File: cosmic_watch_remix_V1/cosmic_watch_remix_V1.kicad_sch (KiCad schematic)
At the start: 26 parts, among them IC1 MICROFJ-60035-TSV-TR1, IC2 LT3461AES6#TRMPBF, J1 Conn_01x05_Female, U1 ADS1115IDGS, U2 LM358

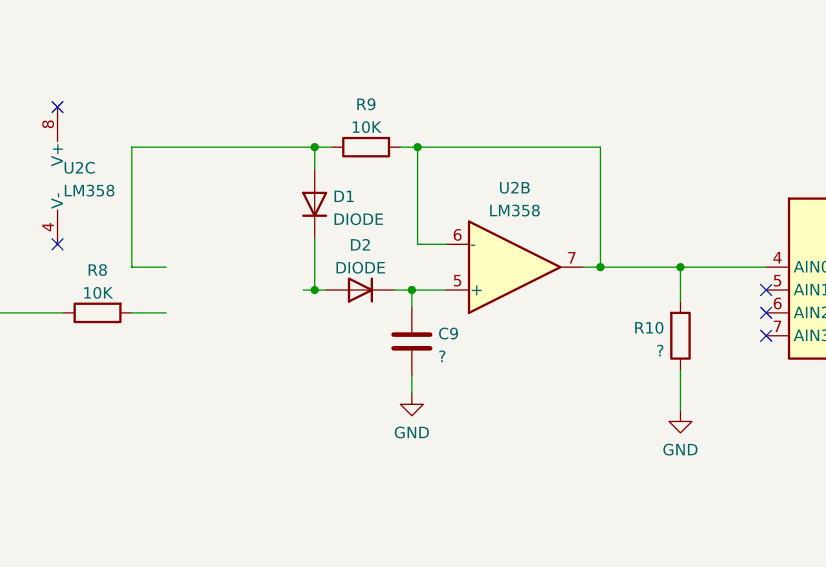
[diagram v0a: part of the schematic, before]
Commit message: Completed Component Selection
Note change to 28V output
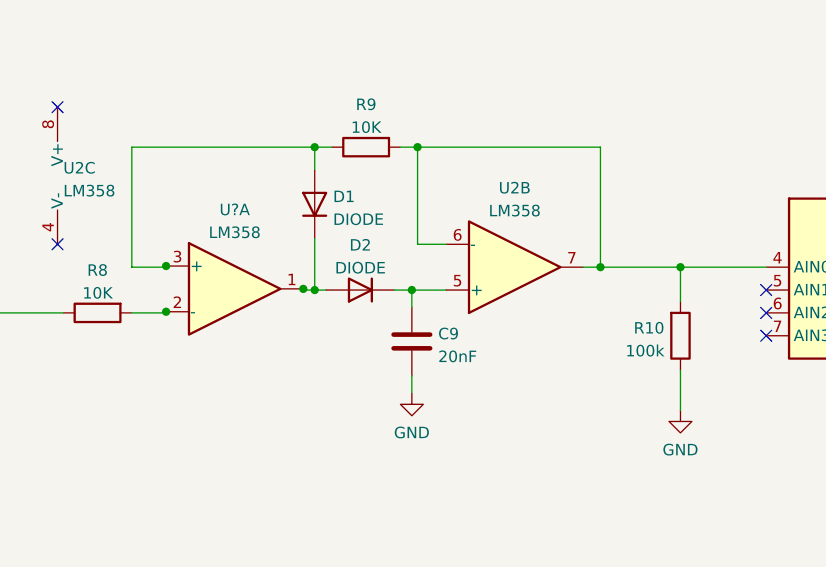
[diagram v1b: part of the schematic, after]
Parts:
- added U?: LM358, symbol Amplifier_Operational:LM358
- C9: value ? -> 20nF
- R10: value ? -> 100k
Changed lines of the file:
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@@
   (junction (at 39.37 128.27) (diameter 0) (color 0 0 0 0)
   )
+  (junction (at 140.97 90.678) (diameter 0) (color 0 0 0 0)
+  )
   (junction (at 99.06 105.41) (diameter 0) (color 0 0 0 0)
   )
@@
   (junction (at 26.035 41.91) (diameter 0) (color 0 0 0 0)
   )
+  (junction (at 125.73 93.218) (diameter 0) (color 0 0 0 0)
+  )
   (junction (at 99.06 135.89) (diameter 0) (color 0 0 0 0)
   )
@@
   )
   (junction (at 33.655 26.67) (diameter 0) (color 0 0 0 0)
+  )
+  (junction (at 125.73 88.138) (diameter 0) (color 0 0 0 0)
   )
   (no_connect (at 192.405 90.805))
@@
     (pin "2")
   )
+  (symbol (lib_id "Amplifier_Operational:LM358") (at 133.35 90.678 0) (unit 1)
+    (in_bom yes) (on_board yes) (fields_autoplaced)
+    (property "Reference" "U?" (id 0) (at 133.35 81.8982 0))
+    (property "Value" "LM358" (id 1) (at 133.35 84.4351 0))
+    (property "Footprint" "" (id 2) (at 133.35 90.678 0)
+      (effects (font (size 1.27 1.27)) hide)
+    )
+    (property "Datasheet" "http://www.ti.com/lit/ds/symlink/lm2904-n.pdf" (id 3) (at 133.35 90.678 0)
+      (effects (font (size 1.27 1.27)) hide)
+    )
+    (pin "1")
+    (pin "2")
+    (pin "3")
+  )
   (symbol (lib_id "power:GND") (at 182.88 104.14 0) (unit 1)
     (in_bom yes) (on_board yes) (fields_autoplaced)
@@
       (effects (font (size 1.27 1.27)) (justify left))
     )
-    (property "Value" "?" (id 1) (at 155.956 98.2222 0)
+    (property "Value" "20nF" (id 1) (at 155.956 98.2222 0)
       (effects (font (size 1.27 1.27)) (justify left))
     )
@@
   (symbol (lib_id "Device:R") (at 182.88 95.885 0) (mirror x) (unit 1)
     (in_bom yes) (on_board yes) (fields_autoplaced)
-    (property "Reference" "R10" (id 0) (at 181.102 95.0503 0)
+    (property "Reference" "R10" (id 0) (at 181.1021 95.0503 0)
       (effects (font (size 1.27 1.27)) (justify right))
     )
-    (property "Value" "?" (id 1) (at 181.102 97.5872 0)
+    (property "Value" "100k" (id 1) (at 181.1021 97.5872 0)
       (effects (font (size 1.27 1.27)) (justify right))
     )
@@
     )
     (path "/8d129ac0-21e8-4168-b5e8-555f7b81464d"
-      (reference "C9") (unit 1) (value "?") (footprint "Capacitor_SMD:C_0603_1608Metric")
+      (reference "C9") (unit 1) (value "20nF") (footprint "Capacitor_SMD:C_0603_1608Metric")
     )
     (path "/10789bbb-c1d1-4df2-bd22-ae0dfea0e3cd"
@@
     )
     (path "/a57db792-acd1-4a7c-9f3f-af8789d22ea8"
-      (reference "R10") (unit 1) (value "?") (footprint "Resistor_SMD:R_0603_1608Metric")
+      (reference "R10") (unit 1) (value "100k") (footprint "Resistor_SMD:R_0603_1608Metric")
     )
     (path "/d4e5a639-c802-4fd5-bd43-bd9483f1fee3"
@@
       (reference "U2") (unit 3) (value "LM358") (footprint "Package_SO:SOIC-8_7.5x5.85mm_P1.27mm")
     )
-  )
+    (path "/2e435b0f-671e-4da0-9b1a-48c487e95e18"
+      (reference "U?") (unit 1) (value "LM358") (footprint "")
+    )
+  )

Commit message: Updated Production Files
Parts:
- C9: value 20nF -> 22nF
- R6: value 280K -> 220K
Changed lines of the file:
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@@
     (in_bom yes) (on_board yes) (fields_autoplaced)
     (property "Reference" "R6" (id 0) (at 47.625 48.6242 90))
-    (property "Value" "280K" (id 1) (at 47.625 51.1611 90))
+    (property "Value" "220K" (id 1) (at 47.625 51.1611 90))
     (property "Footprint" "Resistor_SMD:R_0603_1608Metric" (id 2) (at 47.625 51.562 90)
       (effects (font (size 1.27 1.27)) hide)
@@
       (effects (font (size 1.27 1.27)) (justify left))
     )
-    (property "Value" "20nF" (id 1) (at 155.956 98.2222 0)
+    (property "Value" "22nF" (id 1) (at 155.956 98.2222 0)
       (effects (font (size 1.27 1.27)) (justify left))
     )
@@
     )
     (path "/8d129ac0-21e8-4168-b5e8-555f7b81464d"
-      (reference "C9") (unit 1) (value "20nF") (footprint "Capacitor_SMD:C_0603_1608Metric")
+      (reference "C9") (unit 1) (value "22nF") (footprint "Capacitor_SMD:C_0603_1608Metric")
     )
     (path "/10789bbb-c1d1-4df2-bd22-ae0dfea0e3cd"
@@
     )
     (path "/8c8f7f6f-f151-43d0-b7c2-857bd66addff"
-      (reference "R6") (unit 1) (value "280K") (footprint "Resistor_SMD:R_0603_1608Metric")
+      (reference "R6") (unit 1) (value "220K") (footprint "Resistor_SMD:R_0603_1608Metric")
     )
     (path "/b047d4a8-77a5-43d5-bbbe-e454ef0e254d"

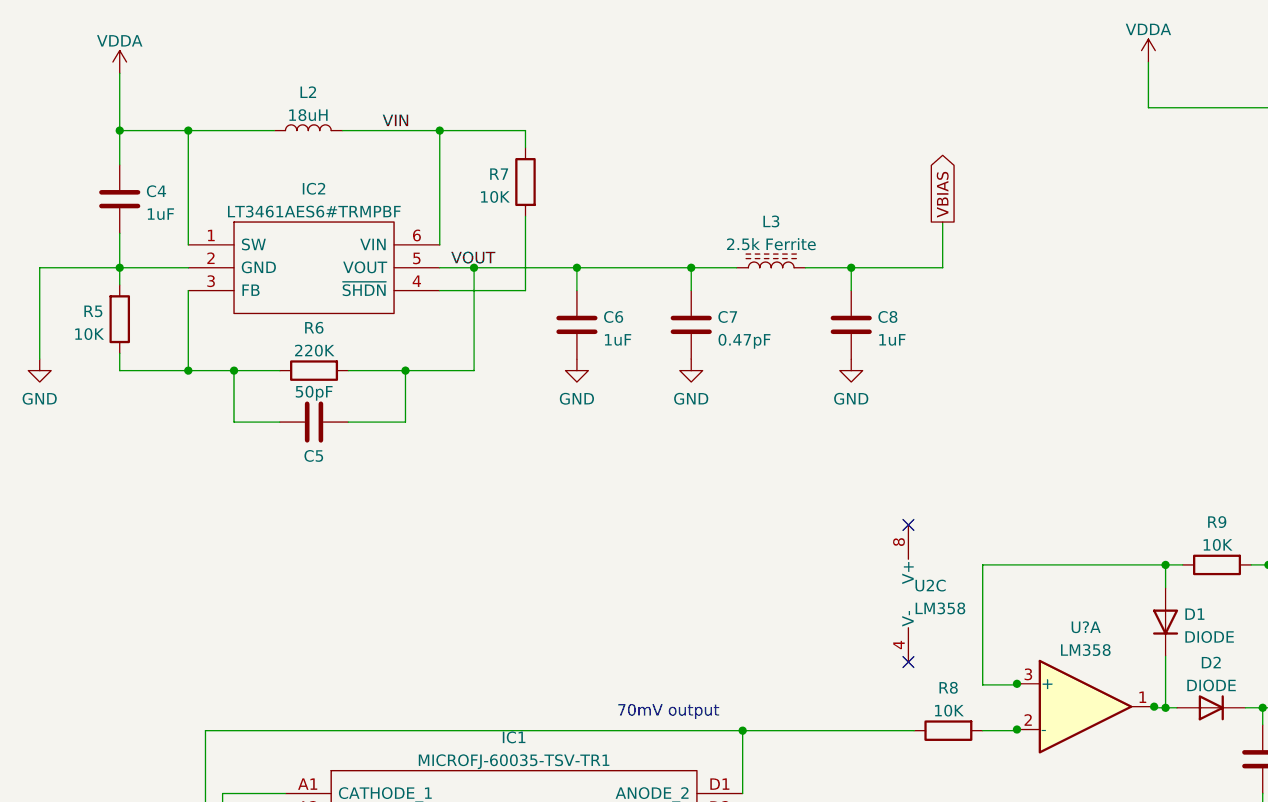
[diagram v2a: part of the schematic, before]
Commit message: Fixed Inductor Power Path
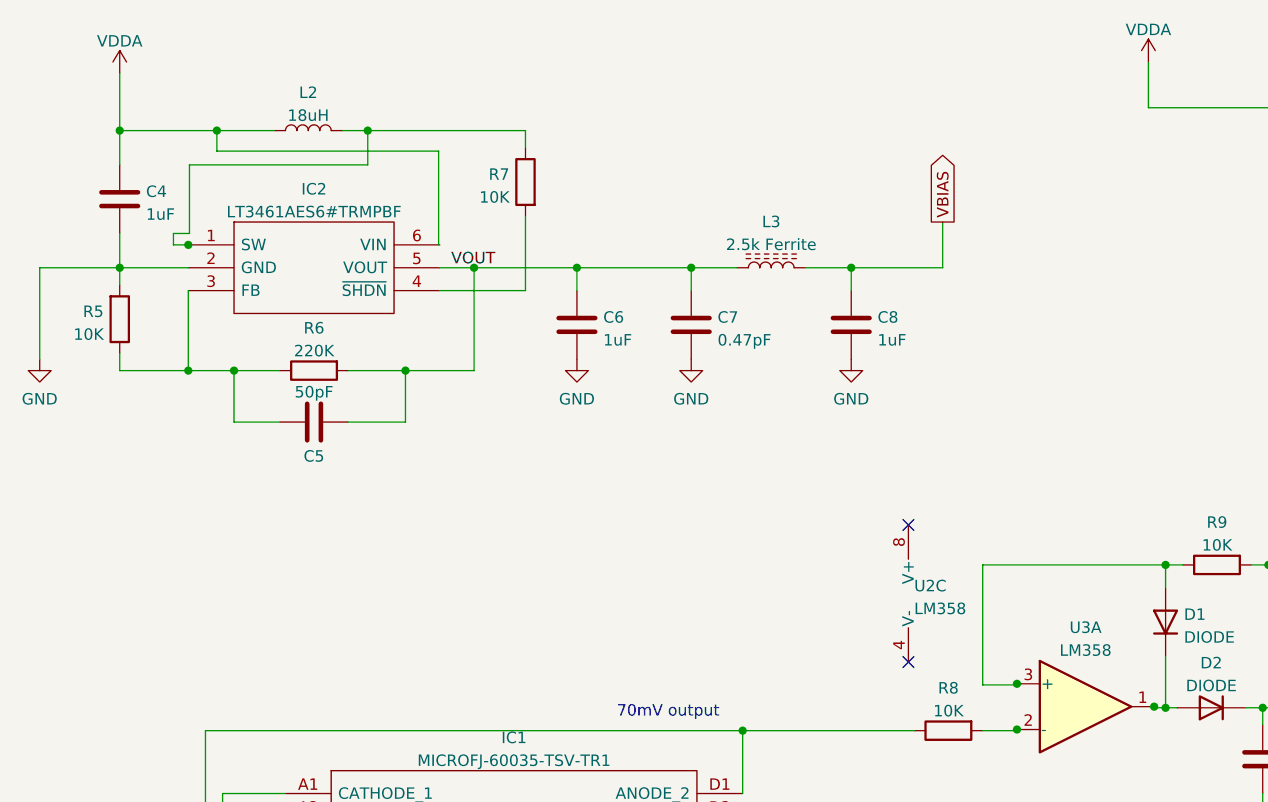
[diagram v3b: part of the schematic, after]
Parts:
- gave numbers to parts that had none: 1
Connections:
- net VCC: no longer IC2.1 (SW)
- net VIN: no longer names the net of L2.2, R7.1
- net VIN: now also IC2.1 (SW); no longer IC2.6 (VIN)
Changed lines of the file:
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@@
   (junction (at 95.25 93.345) (diameter 0) (color 0 0 0 0)
   )
+  (junction (at 33.655 39.37) (diameter 0) (color 0 0 0 0)
+  )
   (junction (at 241.935 93.345) (diameter 0) (color 0 0 0 0)
   )
   (junction (at 39.37 133.35) (diameter 0) (color 0 0 0 0)
   )
-  (junction (at 61.595 26.67) (diameter 0) (color 0 0 0 0)
-  )
   (junction (at 99.06 118.11) (diameter 0) (color 0 0 0 0)
   )
@@
   (junction (at 33.655 53.34) (diameter 0) (color 0 0 0 0)
   )
+  (junction (at 53.594 26.67) (diameter 0) (color 0 0 0 0)
+  )
   (junction (at 99.06 125.73) (diameter 0) (color 0 0 0 0)
   )
@@
   (junction (at 99.06 133.35) (diameter 0) (color 0 0 0 0)
   )
+  (junction (at 36.83 26.67) (diameter 0) (color 0 0 0 0)
+  )
   (junction (at 153.035 90.805) (diameter 0) (color 0 0 0 0)
   )
   (junction (at 173.99 88.265) (diameter 0) (color 0 0 0 0)
-  )
-  (junction (at 33.655 26.67) (diameter 0) (color 0 0 0 0)
   )
   (junction (at 125.73 88.138) (diameter 0) (color 0 0 0 0)
@@
     (stroke (width 0) (type default) (color 0 0 0 0))
   )
+  (wire (pts (xy 33.782 30.48) (xy 33.782 38.1))
+    (stroke (width 0) (type default) (color 0 0 0 0))
+  )
   (wire (pts (xy 39.37 135.89) (xy 39.37 138.43))
     (stroke (width 0) (type default) (color 0 0 0 0))
@@
     (stroke (width 0) (type default) (color 0 0 0 0))
   )
+  (wire (pts (xy 53.594 26.67) (xy 53.594 30.48))
+    (stroke (width 0) (type default) (color 0 0 0 0))
+  )
   (wire (pts (xy 99.06 105.41) (xy 99.06 107.95))
     (stroke (width 0) (type default) (color 0 0 0 0))
@@
     (stroke (width 0) (type default) (color 0 0 0 0))
   )
+  (wire (pts (xy 32.004 38.1) (xy 32.004 39.37))
+    (stroke (width 0) (type default) (color 0 0 0 0))
+  )
   (wire (pts (xy 173.99 74.93) (xy 153.67 74.93))
     (stroke (width 0) (type default) (color 0 0 0 0))
   )
+  (wire (pts (xy 36.83 28.956) (xy 36.83 26.67))
+    (stroke (width 0) (type default) (color 0 0 0 0))
+  )
   (wire (pts (xy 61.595 41.91) (xy 65.405 41.91))
     (stroke (width 0) (type default) (color 0 0 0 0))
@@
     (stroke (width 0) (type default) (color 0 0 0 0))
   )
+  (wire (pts (xy 33.655 39.37) (xy 33.782 39.37))
+    (stroke (width 0) (type default) (color 0 0 0 0))
+  )
   (wire (pts (xy 39.37 120.65) (xy 44.45 120.65))
     (stroke (width 0) (type default) (color 0 0 0 0))
@@
     (stroke (width 0) (type default) (color 0 0 0 0))
   )
-  (wire (pts (xy 71.12 26.67) (xy 61.595 26.67))
+  (wire (pts (xy 50.8 26.67) (xy 53.594 26.67))
+    (stroke (width 0) (type default) (color 0 0 0 0))
+  )
+  (wire (pts (xy 36.83 26.67) (xy 43.18 26.67))
     (stroke (width 0) (type default) (color 0 0 0 0))
   )
@@
     (stroke (width 0) (type default) (color 0 0 0 0))
   )
-  (wire (pts (xy 26.035 26.67) (xy 33.655 26.67))
-    (stroke (width 0) (type default) (color 0 0 0 0))
-  )
   (wire (pts (xy 39.37 110.49) (xy 39.37 113.03))
     (stroke (width 0) (type default) (color 0 0 0 0))
@@
     (stroke (width 0) (type default) (color 0 0 0 0))
   )
-  (wire (pts (xy 61.595 26.67) (xy 61.595 39.37))
-    (stroke (width 0) (type default) (color 0 0 0 0))
-  )
   (wire (pts (xy 95.25 115.57) (xy 99.06 115.57))
     (stroke (width 0) (type default) (color 0 0 0 0))
   )
-  (wire (pts (xy 50.8 26.67) (xy 61.595 26.67))
-    (stroke (width 0) (type default) (color 0 0 0 0))
-  )
   (wire (pts (xy 89.535 41.91) (xy 89.535 44.45))
     (stroke (width 0) (type default) (color 0 0 0 0))
@@
     (stroke (width 0) (type default) (color 0 0 0 0))
   )
-  (wire (pts (xy 33.655 26.67) (xy 43.18 26.67))
+  (wire (pts (xy 53.594 26.67) (xy 71.12 26.67))
+    (stroke (width 0) (type default) (color 0 0 0 0))
+  )
+  (wire (pts (xy 26.035 26.67) (xy 36.83 26.67))
     (stroke (width 0) (type default) (color 0 0 0 0))
   )
@@
     (stroke (width 0) (type default) (color 0 0 0 0))
   )
+  (wire (pts (xy 32.004 39.37) (xy 33.655 39.37))
+    (stroke (width 0) (type default) (color 0 0 0 0))
+  )
   (wire (pts (xy 95.25 105.41) (xy 99.06 105.41))
     (stroke (width 0) (type default) (color 0 0 0 0))
   )
+  (wire (pts (xy 61.468 28.956) (xy 36.83 28.956))
+    (stroke (width 0) (type default) (color 0 0 0 0))
+  )
   (wire (pts (xy 39.37 120.65) (xy 39.37 123.19))
     (stroke (width 0) (type default) (color 0 0 0 0))
@@
     (stroke (width 0) (type default) (color 0 0 0 0))
   )
+  (wire (pts (xy 33.782 38.1) (xy 32.004 38.1))
+    (stroke (width 0) (type default) (color 0 0 0 0))
+  )
   (wire (pts (xy 95.25 100.33) (xy 95.25 93.345))
     (stroke (width 0) (type default) (color 0 0 0 0))
@@
     (stroke (width 0) (type default) (color 0 0 0 0))
   )
+  (wire (pts (xy 61.468 39.37) (xy 61.468 28.956))
+    (stroke (width 0) (type default) (color 0 0 0 0))
+  )
   (wire (pts (xy 39.37 138.43) (xy 44.45 138.43))
     (stroke (width 0) (type default) (color 0 0 0 0))
@@
     (stroke (width 0) (type default) (color 0 0 0 0))
   )
+  (wire (pts (xy 53.594 30.48) (xy 33.782 30.48))
+    (stroke (width 0) (type default) (color 0 0 0 0))
+  )
   (wire (pts (xy 178.435 24.13) (xy 178.435 19.05))
     (stroke (width 0) (type default) (color 0 0 0 0))
@@
   )
   (wire (pts (xy 95.25 107.95) (xy 99.06 107.95))
-    (stroke (width 0) (type default) (color 0 0 0 0))
-  )
-  (wire (pts (xy 33.655 39.37) (xy 33.655 26.67))
     (stroke (width 0) (type default) (color 0 0 0 0))
   )
@@
   )
   (label "VOUT" (at 62.865 41.91 0)
-    (effects (font (size 1.27 1.27)) (justify left bottom))
-  )
-  (label "VIN" (at 55.245 26.67 0)
     (effects (font (size 1.27 1.27)) (justify left bottom))
   )
@@
       (effects (font (size 1.27 1.27)) hide)
     )
+    (pin "1")
+    (pin "2")
+    (pin "3")
+    (pin "5")
+    (pin "6")
+    (pin "7")
     (pin "4")
     (pin "8")
@@
   (symbol (lib_id "Amplifier_Operational:LM358") (at 133.35 90.678 0) (unit 1)
     (in_bom yes) (on_board yes) (fields_autoplaced)
-    (property "Reference" "U?" (id 0) (at 133.35 81.8982 0))
+    (property "Reference" "U3" (id 0) (at 133.35 81.8982 0))
     (property "Value" "LM358" (id 1) (at 133.35 84.4351 0))
     (property "Footprint" "" (id 2) (at 133.35 90.678 0)
@@
     (pin "2")
     (pin "3")
+    (pin "5")
+    (pin "6")
+    (pin "7")
+    (pin "4")
+    (pin "8")
   )
   (symbol (lib_id "power:GND") (at 182.88 104.14 0) (unit 1)
@@
       (effects (font (size 1.27 1.27)) hide)
     )
+    (pin "1")
+    (pin "2")
+    (pin "3")
     (pin "5")
     (pin "6")
     (pin "7")
+    (pin "4")
+    (pin "8")
   )
   (symbol (lib_id "Device:R") (at 182.88 95.885 0) (mirror x) (unit 1)
@@
     )
     (path "/2e435b0f-671e-4da0-9b1a-48c487e95e18"
-      (reference "U?") (unit 1) (value "LM358") (footprint "")
-    )
-  )
+      (reference "U3") (unit 1) (value "LM358") (footprint "")
+    )
+  )
